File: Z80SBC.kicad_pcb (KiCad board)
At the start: 2 copper layers, 208 x 115 mm, 100 parts, among them IC1 SIO2-DIP-40, IC2 Z80CPU-DIP, J1 PH, J10 Conn_01x01, J11 Conn_01x01, J12 Conn_01x01, J2 DB9_Female, J3 CFCONN, J4 Barrel_Jack, J5 Conn_01x10, J6 Conn_01x10, J7 Conn_01x10, J8 Conn_01x08, J9 Conn_01x01, SW1 SW_Push, SW2 SW_Push, U1 MAX232_ALT, U10 74HCT32, U11 74HCT00, U12 74HC393, U13 74HC595, U14 74HC165, U15 MicroSD_SPI_CD, U16 MicroSD_SPI_CD, U2 74LS138, U3 628128, U4 28C256, U5 LM7805, U6 74HCT32, U7 74HCT00, U8 74HCT32, U9 8255A, Y1 7.3728 MHz, Y2 16 MHz

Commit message: Added PS/2 keyboard input
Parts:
- added C31: 100 nF, Capacitors_THT:C_Disc_D5.0mm_W2.5mm_P2.50mm, F.Cu at (33.2, 137.7)
- added D8: 1N4148, Diodes_THT:D_DO-35_SOD27_P7.62mm_Horizontal, F.Cu at (123.0, 107.2)
- added J13: Conn_01x04, Pin_Headers:Pin_Header_Straight_1x04_Pitch2.54mm, F.Cu at (69.2, 134.2)
- added P1: Mini-DIN_6pins_ver4, Z80:Connector_Mini-DIN_Female_6Pin_2rows, F.Cu at (46.9, 131.2)
- added R24: 1k, Resistors_THT:R_Axial_DIN0207_L6.3mm_D2.5mm_P7.62mm_Horizontal, F.Cu at (123.6, 136.8)
- added R25: 1k, Resistors_THT:R_Axial_DIN0207_L6.3mm_D2.5mm_P7.62mm_Horizontal, F.Cu at (43.2, 119.1)
- added R26: 10k, Resistors_THT:R_Axial_DIN0207_L6.3mm_D2.5mm_P7.62mm_Horizontal, F.Cu at (36.8, 115.7)
- added R27: 10k, Resistors_THT:R_Axial_DIN0207_L6.3mm_D2.5mm_P7.62mm_Horizontal, F.Cu at (40.0, 115.7)
- added R28: 1k, Resistors_THT:R_Axial_DIN0207_L6.3mm_D2.5mm_P7.62mm_Horizontal, F.Cu at (43.2, 115.8)
- moved R5 26.2 mm to (75.7, 127.8), turned to 0 degrees
- moved R7 25.3 mm to (129.8, 113.9), turned to 180 degrees
- moved R8 23.4 mm to (129.8, 110.7), turned to 180 degrees
- moved D3 19.3 mm to (104.8, 101.2), turned to 180 degrees
- moved R11 17.6 mm to (29.6, 117.5)
- moved R21 17.6 mm to (33.0, 117.4)
- moved R12 17.6 mm to (29.7, 134.9)
- moved R4 17.5 mm to (75.8, 124.6), turned to 0 degrees
- moved R22 17.5 mm to (33.0, 134.9)
- moved R10 15.6 mm to (116.9, 107.7), turned to 180 degrees
- moved C25 14.2 mm to (103.0, 105.4), turned to 180 degrees
- moved J3 1.40 mm to (87.0, 113.3)
- moved C9 0.54 mm to (127.1, 117.1), turned to 0 degrees
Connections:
- D3 pad 2: Net-(D3-Pad2) -> +5V
- J3 pad 45: Net-(D3-Pad1) -> Net-(J3-Pad45)
- R10 pad 1: Net-(D3-Pad2) -> Net-(J3-Pad45)
- R10 pad 2: +5V -> Net-(D3-Pad1)
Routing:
- net Net-(J13-Pad2): track 0.00 -> 99.9 mm
- net +5V: track 941.6 -> 1006.9 mm, vias 22 -> 21
- net Net-(J13-Pad3): track 0.00 -> 52.7 mm
- net Net-(J3-Pad45): track 0.00 -> 26.6 mm
- net Net-(D8-Pad1): track 0.00 -> 22.7 mm
- net Net-(J3-Pad36): track 6.36 -> 27.1 mm, vias 0 -> 2
- net Net-(J6-Pad3): track 15.2 -> 32.5 mm, vias 0 -> 1
- net Net-(J6-Pad2): track 17.2 -> 32.1 mm, vias 0 -> 1
- net Net-(J7-Pad3): track 29.4 -> 44.4 mm
- net Net-(P1-Pad7): track 0.00 -> 14.4 mm
- net Net-(J7-Pad2): track 34.5 -> 48.0 mm
- net SDCS2: track 92.9 -> 79.8 mm
- net Net-(J3-Pad32): track 8.50 -> 21.3 mm
- net SDCS: track 112.3 -> 101.2 mm
- net INT: track 71.7 -> 79.0 mm
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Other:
- board text added: "CLK"
- board text added: "DAT"
- board text added: "PS/2 KYBD"
- board text added: "SIOA"
- board text added: "SIOB"

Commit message: Added ESP-01 and video output
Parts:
- added C32: 100 nF, Capacitors_THT:C_Disc_D5.0mm_W2.5mm_P2.50mm, F.Cu at (211.9, 50.2)
- added D10: 1N4148, Diodes_THT:D_DO-35_SOD27_P7.62mm_Horizontal, F.Cu at (214.2, 29.9)
- added D9: 1N4148, Diodes_THT:D_DO-35_SOD27_P7.62mm_Horizontal, F.Cu at (214.2, 27.1)
- added J14: RCAJack, Z80:RCAConnectorCommon, F.Cu at (24.8, 125.7)
- added J15: Conn_02x04_Odd_Even, Z80:Pin_Header_Straight_2x04_Pitch2.54mm_Flipped, F.Cu at (220.3, 39.7)
- added JP7: Jumper_NC_Dual, Pin_Headers:Pin_Header_Straight_1x03_Pitch2.54mm, F.Cu at (90.6, 55.1)
- added R29: 82R, Resistors_THT:R_Axial_DIN0207_L6.3mm_D2.5mm_P7.62mm_Horizontal, F.Cu at (20.4, 117.5)
- added R30: 1k, Resistors_THT:R_Axial_DIN0207_L6.3mm_D2.5mm_P7.62mm_Horizontal, F.Cu at (21.4, 114.8)
- added R31: 470R, Resistors_THT:R_Axial_DIN0207_L6.3mm_D2.5mm_P7.62mm_Horizontal, F.Cu at (24.7, 114.7)
- added R32: 470R, Resistors_THT:R_Axial_DIN0207_L6.3mm_D2.5mm_P7.62mm_Horizontal, F.Cu at (209.3, 47.6)
- added R33: 1k, Resistors_THT:R_Axial_DIN0207_L6.3mm_D2.5mm_P7.62mm_Horizontal, F.Cu at (212.7, 47.6)
- IC1: value SIO2-DIP-40 -> DART-DIP-40
- R24: value 1k -> 100R
- moved C18 4.96 mm to (114.3, 47.9)
- moved R11 2.30 mm to (31.9, 116.8)
- moved R22 2.26 mm to (35.2, 134.8)
- moved R12 2.24 mm to (31.9, 134.9)
- moved R21 2.18 mm to (35.1, 116.8)
- moved R26 1.64 mm to (38.4, 115.8)
- moved R27 1.59 mm to (41.6, 115.8)
- moved R28 1.03 mm to (44.2, 115.8)
- moved R25 1.01 mm to (44.2, 119.1)
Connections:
- IC1 pad 28: CLK -> RXDB
- IC1 pad 29: RXDB -> (no net)
- IC1 pad 31: (no net) -> GND
- P1 pad 7: Net-(P1-Pad7) -> GND
- U11 pad 4: +5V -> Net-(C17-Pad1)
- U4 pad 1: A14 -> R14
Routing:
- net Net-(J7-Pad9): track 7.88 -> 152.0 mm, vias 0 -> 2
- net Net-(IC1-Pad12): track 6.35 -> 75.6 mm, vias 0 -> 4
- net Net-(IC1-Pad15): track 7.10 -> 61.7 mm, vias 0 -> 4
- net Net-(C32-Pad1): track 0.00 -> 43.6 mm
- net +5V: track 1006.9 -> 1033.8 mm
- net Net-(J15-Pad7): track 0.00 -> 21.6 mm
- net R14: track 0.00 -> 15.6 mm
- net Net-(P1-Pad7): track 14.4 -> 0.00 mm
- net Net-(J14-Pad2): track 0.00 -> 11.7 mm
- net MOSI: track 62.9 -> 71.8 mm
- net Net-(D10-Pad2): track 0.00 -> 8.86 mm
- net Net-(R29-Pad2): track 0.00 -> 7.91 mm
- net SDCS2: track 79.8 -> 83.5 mm
- net Net-(J13-Pad3): track 52.7 -> 49.4 mm
- net Net-(J7-Pad3): track 44.4 -> 41.2 mm
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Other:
- board text added: "ESP-01"
- board text added: "LOW 16K"
- board text added: "UPR 16K"
- board text added: "Z80 DART"
- board text added: "Z80 SBC LAYOUT BY DANIEL MARKS"
- board text removed: "SIO/2 DART"
- board text removed: "Z80 SBC LAYOUT BY DANIEL MARS"

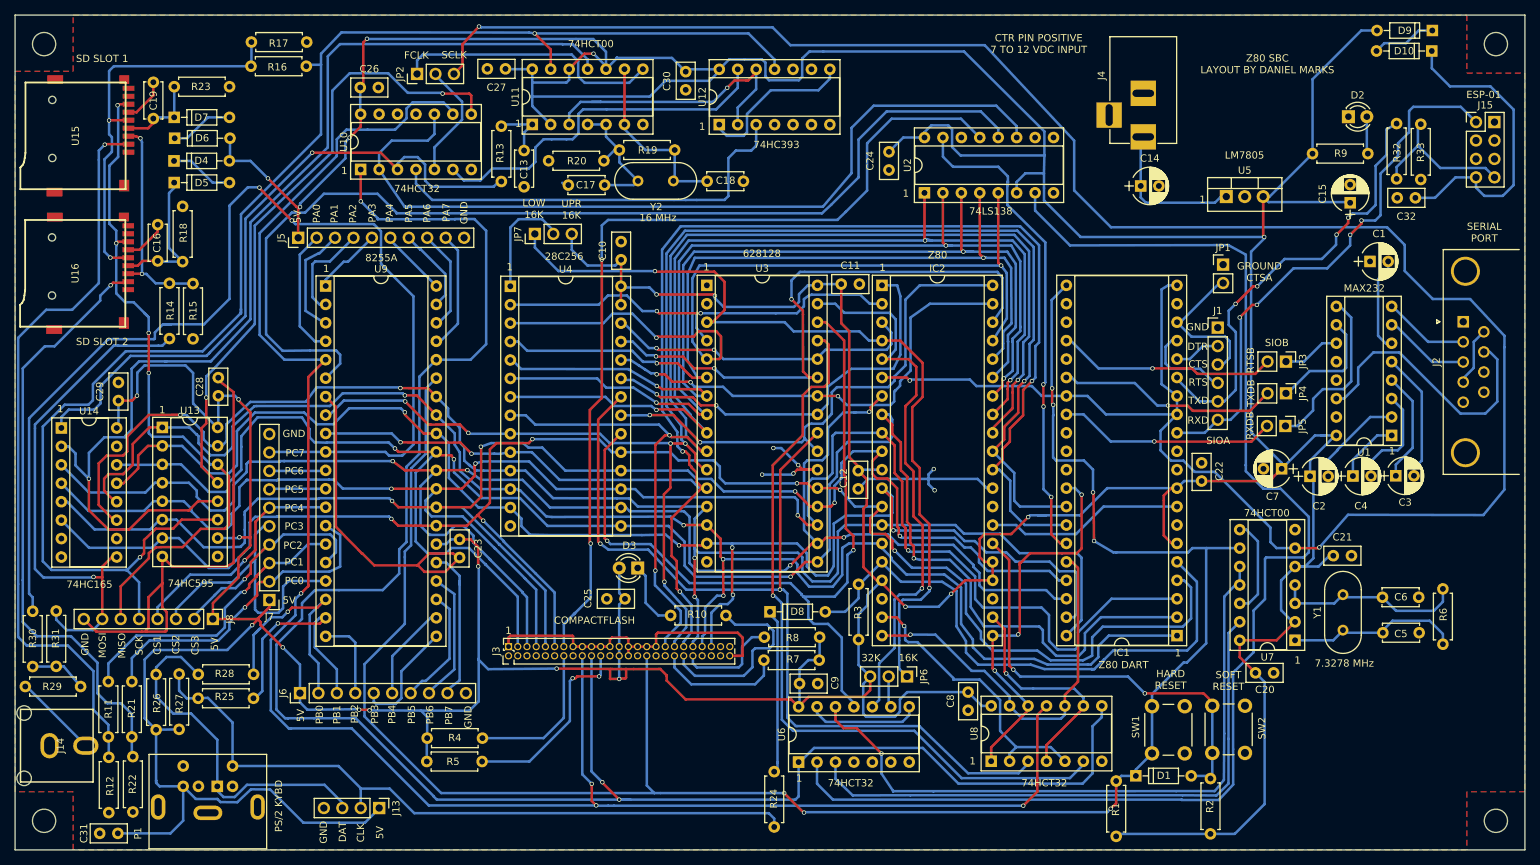
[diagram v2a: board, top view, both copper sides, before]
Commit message: Fixed jumpers, CF card position, ESP-01 enable
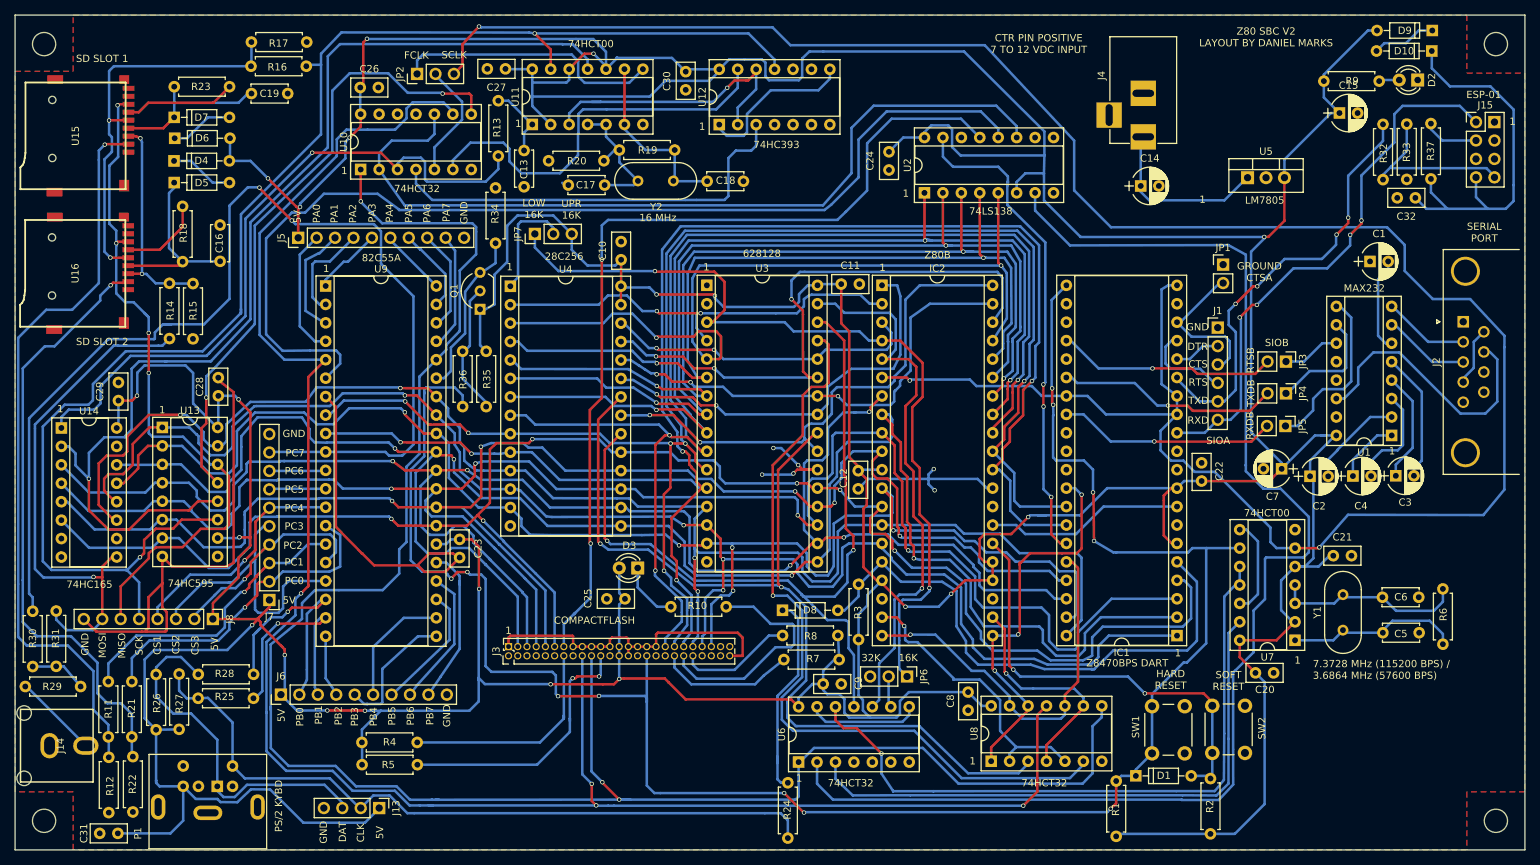
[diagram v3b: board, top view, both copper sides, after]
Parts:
- added Q1: 2N3906, TO_SOT_Packages_THT:TO-92_Inline_Wide, F.Cu at (83.1, 65.5)
- added R34: 10k, Resistors_THT:R_Axial_DIN0207_L6.3mm_D2.5mm_P7.62mm_Horizontal, F.Cu at (85.2, 48.8)
- added R35: 100k, Resistors_THT:R_Axial_DIN0207_L6.3mm_D2.5mm_P7.62mm_Horizontal, F.Cu at (83.9, 78.9)
- added R36: 10k, Resistors_THT:R_Axial_DIN0207_L6.3mm_D2.5mm_P7.62mm_Horizontal, F.Cu at (80.7, 78.9)
- added R37: 10k, Resistors_THT:R_Axial_DIN0207_L6.3mm_D2.5mm_P7.62mm_Horizontal, F.Cu at (214.1, 40.0)
- R32: value 470R -> 4k7
- R33: value 1k -> 10k
- moved C19 13.9 mm to (51.6, 35.8), turned to 0 degrees
- moved C15 12.4 mm to (201.4, 38.5), turned to 0 degrees
- moved D2 10.8 mm to (212.2, 34.0), turned to 180 degrees
- moved R9 10.1 mm to (206.9, 34.1)
- moved R4 9.01 mm to (66.8, 125.2)
- moved R5 8.93 mm to (66.8, 128.3)
- moved C16 8.59 mm to (47.2, 58.9)
- moved U5 3.92 mm to (188.8, 47.4)
- moved R13 3.54 mm to (85.6, 44.4)
- moved C9 3.25 mm to (130.3, 117.2)
- moved R7 2.75 mm to (132.5, 113.8)
- moved J6 2.63 mm to (55.6, 118.6)
- moved R8 2.52 mm to (132.3, 110.5)
- moved R24 2.42 mm to (125.5, 138.4)
- moved R33 1.93 mm to (210.7, 47.6)
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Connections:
- IC1 pad 10: (no net) -> Net-(IC1-Pad10)
- IC1 pad 11: (no net) -> Net-(IC1-Pad11)
- IC1 pad 25: (no net) -> Net-(IC1-Pad25)
- IC1 pad 29: (no net) -> Net-(IC1-Pad29)
- IC1 pad 30: (no net) -> Net-(IC1-Pad30)
- IC1 pad 7: (no net) -> Net-(IC1-Pad7)
- IC2 pad 18: (no net) -> Net-(IC2-Pad18)
- IC2 pad 23: (no net) -> Net-(IC2-Pad23)
- IC2 pad 28: (no net) -> Net-(IC2-Pad28)
- J10 pad 1: (no net) -> Net-(J10-Pad1)
- J11 pad 1: (no net) -> Net-(J11-Pad1)
- J12 pad 1: (no net) -> Net-(J12-Pad1)
- J15 pad 3: (no net) -> Net-(J15-Pad3)
- J15 pad 4: (no net) -> Net-(J15-Pad4)
- J15 pad 5: (no net) -> Net-(J15-Pad5)
- J15 pad 6: (no net) -> Net-(J15-Pad6)
- J2 pad 1: (no net) -> Net-(J2-Pad1)
- J2 pad 8: (no net) -> Net-(J2-Pad8)
- J2 pad 9: (no net) -> Net-(J2-Pad9)
- J3 pad 24: (no net) -> Net-(J3-Pad24)
- J3 pad 25: (no net) -> Net-(J3-Pad25)
- J3 pad 26: (no net) -> Net-(J3-Pad26)
- J3 pad 27: (no net) -> Net-(J3-Pad27)
- J3 pad 28: (no net) -> Net-(J3-Pad28)
- J3 pad 29: (no net) -> Net-(J3-Pad29)
- J3 pad 30: (no net) -> Net-(J3-Pad30)
- J3 pad 31: (no net) -> Net-(J3-Pad31)
- J3 pad 33: (no net) -> Net-(J3-Pad33)
- J3 pad 37: (no net) -> Net-(J3-Pad37)
- J3 pad 40: (no net) -> Net-(J3-Pad40)
- J3 pad 42: (no net) -> Net-(J3-Pad42)
- J3 pad 43: (no net) -> Net-(J3-Pad43)
- J3 pad 47: (no net) -> Net-(J3-Pad47)
- J3 pad 48: (no net) -> Net-(J3-Pad48)
- J3 pad 49: (no net) -> Net-(J3-Pad49)
- J4 pad 3: (no net) -> Net-(J4-Pad3)
- J9 pad 1: (no net) -> Net-(J9-Pad1)
- JP6 pad 3: +5V -> GND
- P1 pad 2: (no net) -> Net-(P1-Pad2)
- P1 pad 6: (no net) -> Net-(P1-Pad6)
- U1 pad 12: (no net) -> Net-(U1-Pad12)
- U1 pad 13: (no net) -> Net-(U1-Pad13)
- U10 pad 11: (no net) -> Net-(U10-Pad11)
- U12 pad 10: (no net) -> Net-(U12-Pad10)
- U12 pad 4: (no net) -> Net-(U12-Pad4)
- U12 pad 5: (no net) -> Net-(U12-Pad5)
- U12 pad 6: (no net) -> Net-(U12-Pad6)
- U12 pad 9: (no net) -> Net-(U12-Pad9)
- U13 pad 9: (no net) -> Net-(U13-Pad9)
- U14 pad 7: (no net) -> Net-(U14-Pad7)
- U15 pad 9: (no net) -> Net-(U15-Pad9)
- U16 pad 9: (no net) -> Net-(U16-Pad9)
- U2 pad 10: (no net) -> IO28-2F
- U2 pad 14: (no net) -> IO08-0F
- U2 pad 9: (no net) -> IO30-37
- U6 pad 6: (no net) -> Net-(U6-Pad6)
- U9 pad 35: COLDRESET -> Net-(Q1-Pad3)
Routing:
- net Net-(Q1-Pad3): track 0.00 -> 22.8 mm
- net Net-(Q1-Pad2): track 0.00 -> 19.7 mm
- net +5V: track 1033.8 -> 1048.7 mm
- net GND: track 211.3 -> 226.1 mm
- net COLDRESET: track 283.0 -> 270.1 mm, vias 7 -> 11
- net Net-(C19-Pad1): track 11.5 -> 22.3 mm
- net Net-(J3-Pad36): track 27.1 -> 37.5 mm
- net Net-(C32-Pad1): track 43.6 -> 53.3 mm
- net Net-(J3-Pad32): track 21.3 -> 30.5 mm
- net Net-(J15-Pad4): track 0.00 -> 7.62 mm
- net Net-(D8-Pad1): track 22.7 -> 29.4 mm
- net Net-(J3-Pad45): track 26.6 -> 32.3 mm
- net Net-(C16-Pad1): track 19.8 -> 24.9 mm
- net IORD!: track 258.7 -> 263.4 mm
- net Net-(U10-Pad6): track 50.4 -> 55.0 mm
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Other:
- board text added: "7.3728 MHz (115200 BPS) / 3.6864 MHz (57600 BPS)"
- board text added: "82C55A"
- board text added: "Z80 SBC V2 LAYOUT BY DANIEL MARKS"
- board text added: "Z80B"
- board text added: "Z8470BPS DART"
- board text removed: "7.3278 MHz"
- board text removed: "8255A"
- board text removed: "Z80"
- board text removed: "Z80 DART"
- board text removed: "Z80 SBC LAYOUT BY DANIEL MARKS"

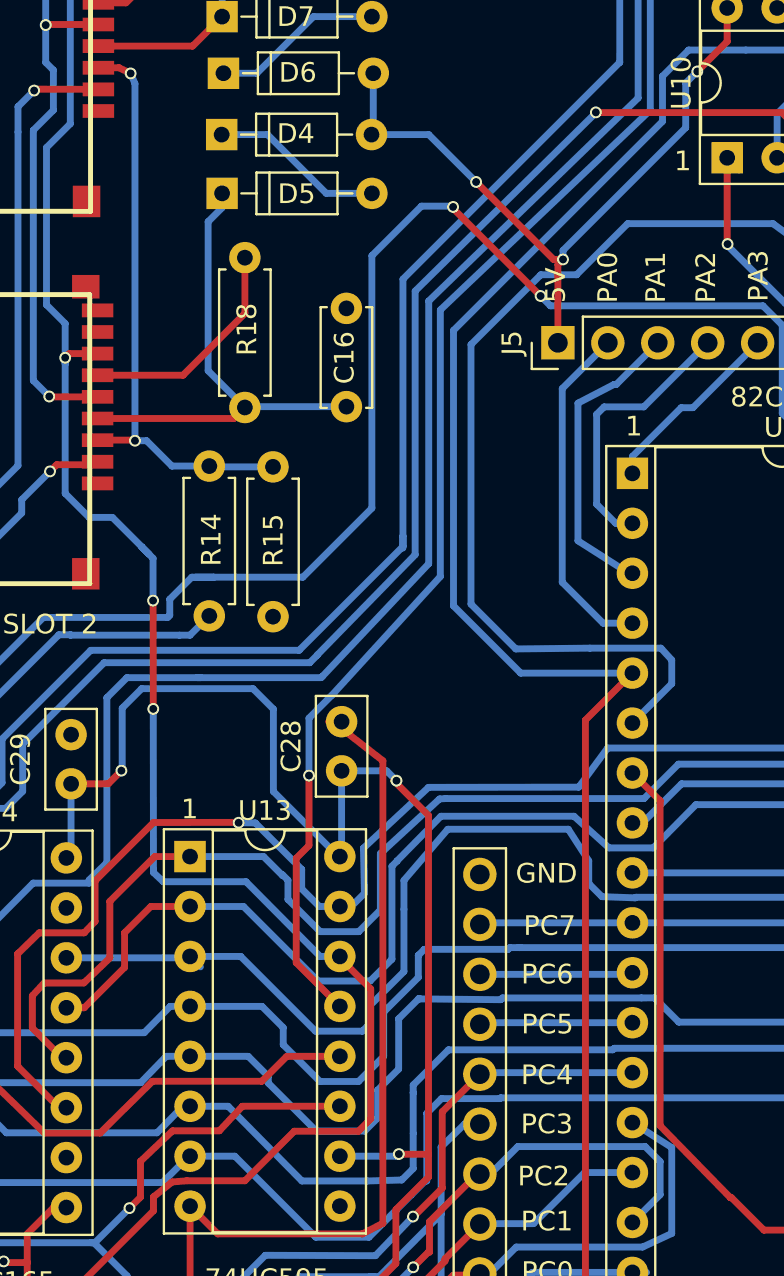
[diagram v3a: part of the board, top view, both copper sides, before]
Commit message: Added SD card driver
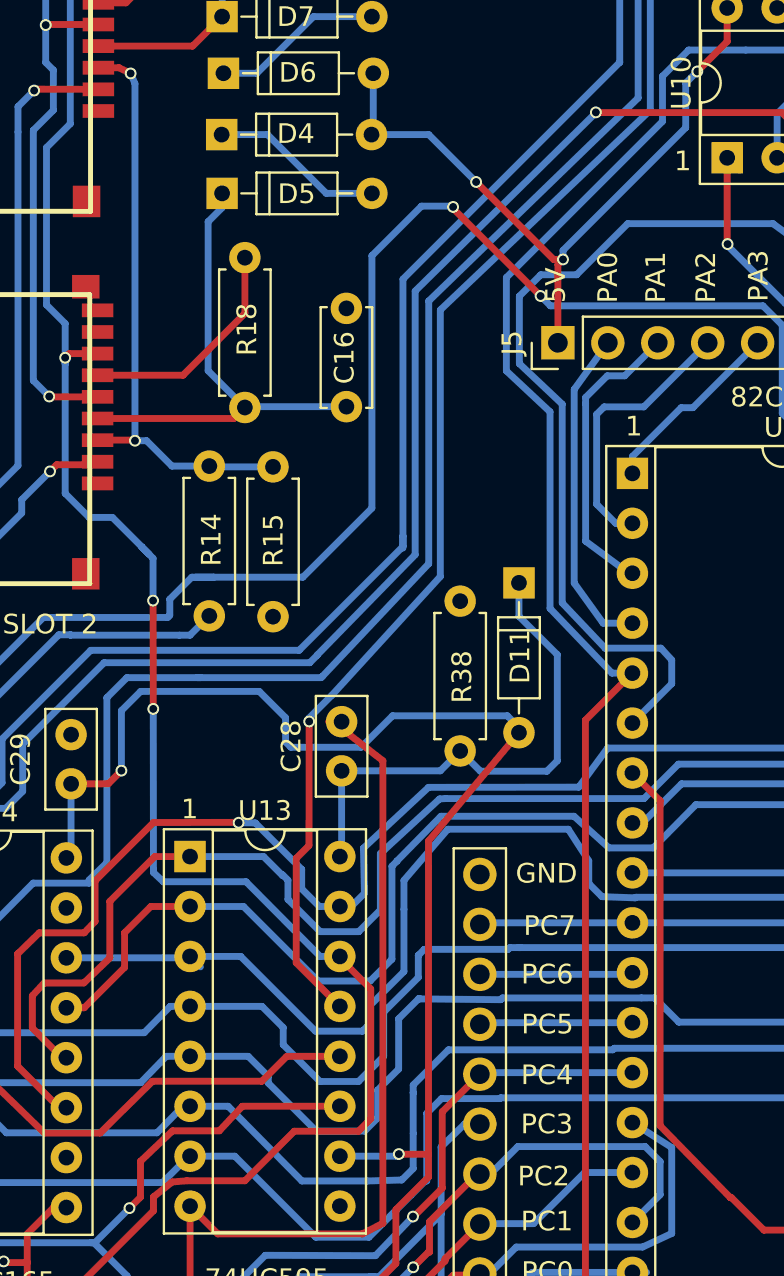
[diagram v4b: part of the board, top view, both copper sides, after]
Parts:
- added D11: 1N4148, Diodes_THT:D_DO-35_SOD27_P7.62mm_Horizontal, F.Cu at (56.0, 67.9)
- added R38: 1k, Resistors_THT:R_Axial_DIN0207_L6.3mm_D2.5mm_P7.62mm_Horizontal, F.Cu at (53.0, 68.8)
- U13: value 74HC595 -> 74HC595pwr
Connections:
- C28 pad 1: +5V -> Net-(C28-Pad1)
- U13 pad 16: +5V -> Net-(C28-Pad1)
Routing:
- net Net-(C28-Pad1): track 0.00 -> 26.4 mm
- net IORD!: track 263.4 -> 258.5 mm
- net IO18-1F: track 143.7 -> 138.9 mm
- net +5V: track 1048.7 -> 1050.7 mm, vias 21 -> 20
- net Net-(J5-Pad2): track 17.5 -> 16.7 mm

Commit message: Fixed PS/2 interrupt line
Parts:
- removed D8: 1N4148, Diodes_THT:D_DO-35_SOD27_P7.62mm_Horizontal
- removed R24: 100R, Resistors_THT:R_Axial_DIN0207_L6.3mm_D2.5mm_P7.62mm_Horizontal
- added JP8: PH, Pin_Headers:Pin_Header_Straight_1x02_Pitch2.54mm, F.Cu at (192.5, 76.5)
- added JP9: Jumper_NC_Dual, Pin_Headers:Pin_Header_Straight_1x03_Pitch2.54mm, F.Cu at (200.2, 62.5)
- JP5: value PH -> Jumper_NC_Dual; footprint Pin_Headers:Pin_Header_Straight_1x02_Pitch2.54mm -> Pin_Headers:Pin_Header_Straight_1x03_Pitch2.54mm
- R11, R21: value 470R -> 4k7
- R12, R22: value 1k -> 10k
- moved C7 13.2 mm to (205.1, 93.8)
- moved C2 12.2 mm to (208.4, 93.8)
- moved C4 12.1 mm to (214.2, 93.8)
- moved C3 12.0 mm to (219.9, 93.9)
- moved R2 10.7 mm to (191.0, 130.0), turned to 180 degrees
- moved D1 10.1 mm to (172.5, 119.8), turned to 270 degrees
- moved JP5 8.19 mm to (192.5, 89.7), turned to 180 degrees
- moved C1 7.71 mm to (212.9, 61.7), turned to 180 degrees
- moved R1 7.40 mm to (178.0, 137.0)
- moved JP3 6.13 mm to (197.1, 67.4)
- moved JP4 5.60 mm to (197.1, 72.4)
- moved U1 4.18 mm to (211.3, 86.1)
- moved C22 2.26 mm to (182.6, 91.4), turned to 270 degrees
- moved JP1 0.80 mm to (184.7, 59.1)
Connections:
- IC1 pad 11: Net-(IC1-Pad11) -> SYNCA
- IC1 pad 23: GND -> CTSB
- IC1 pad 29: Net-(IC1-Pad29) -> RXDBSIO2
- J13 pad 2: Net-(J13-Pad2) -> SYNCA
- JP5 pad 1: Net-(JP5-Pad1) -> RXDBSIO2
- JP5 pad 2: RXDB -> Net-(JP5-Pad2)
- P1 pad 5: Net-(J13-Pad2) -> SYNCA
- R25 pad 1: Net-(J13-Pad2) -> SYNCA
- R27 pad 1: Net-(J13-Pad2) -> SYNCA
- U1 pad 13: Net-(U1-Pad13) -> Net-(J2-Pad8)
- U1 pad 9: Net-(JP5-Pad1) -> Net-(JP5-Pad2)
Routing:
- net SYNCA: track 0.00 -> 218.3 mm, vias 0 -> 4
- net Net-(J13-Pad2): track 101.0 -> 0.00 mm
- net +5V: track 1050.7 -> 1129.0 mm, vias 20 -> 21
- net GND: track 226.1 -> 292.2 mm
- net CTSB: track 0.00 -> 52.5 mm, vias 0 -> 2
- net RXDBSIO2: track 0.00 -> 36.3 mm, vias 0 -> 1
- net Net-(D8-Pad1): track 29.4 -> 0.00 mm
- net COLDRESET: track 270.1 -> 299.3 mm
- net Net-(JP5-Pad2): track 0.00 -> 25.9 mm
- net Net-(JP5-Pad1): track 24.1 -> 0.00 mm
- net Net-(J2-Pad8): track 0.00 -> 22.2 mm
- net Net-(JP9-Pad3): track 0.00 -> 17.9 mm
- net CLK: track 322.1 -> 338.5 mm
- net Net-(J2-Pad7): track 38.7 -> 22.4 mm, vias 0 -> 1
- net Net-(JP3-Pad1): track 8.78 -> 20.7 mm
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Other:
- board text added: "AUX CLK"
- board text added: "CLOSE SIO/2"
- board text added: "CPU CLK"
- board text added: "CTSB"
- board text added: "DART"
- board text added: "PORT"
- board text added: "SIO/2"
- board text removed: "FCLK"
- board text removed: "SCLK"
